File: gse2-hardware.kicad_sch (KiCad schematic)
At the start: 77 parts, among them J1 PJ-002A, J16 ARM, J17 ALARM, J2 PJ-002A, J3 ARM Cortex Debug, J31 Conn_02x09_Top_Bottom, J4 USB-C, Q15 DMG3402L, U27 USBLC6-2SC6, U36 MP2338GTL-Z, Y1 16MHz

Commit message: GSE v2.1: Updates for DSUB connectors for schematic only done. Layout needs a ton of work
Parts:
- removed D1: SDT8A100P5-7, Diode_SMD:D_PowerDI-5, symbol Device:D_Schottky_Small
- removed J17: ALARM, 0UCIRP-KiCAD-Lib:GX-16 2 pin, symbol Connector:Conn_01x02_Pin
- added C27: 0.1uF, Capacitor_SMD:C_0603_1608Metric, symbol Device:C_Small
- added C28: 100nF, Capacitor_SMD:C_0603_1608Metric, symbol Device:C_Small
- added D3: FSV8100V, Diode_SMD:D_PowerDI-5, symbol Device:D_Schottky_Small
- added J47: DSUB_15pin/VGA Veritical Female, 0UCIRP-KiCAD-Lib:Connector_VGA_Vertical, symbol 0UCIRP-KiCAD-Lib:Connector_VGA_vertical
- added R23, R24: 0R, Resistor_SMD:R_1210_3225Metric_Pad1.30x2.65mm_HandSolder, symbol Device:R_Small_US
- added R26: 2k, Resistor_SMD:R_0603_1608Metric, symbol Device:R_Small_US
- added U8: MAX11614, Package_SO:QSOP-16_3.9x4.9mm_P0.635mm, symbol Analog_ADC:MAX11614
- D4: value SDT8A100P5-7 -> FSV8100V
- F1: value ~ -> 3568
- J7: renamed from J31; value Conn_02x09_Top_Bottom -> 0430451812
- U1: renamed from U2; value ~ -> STM32F105RCT6
- U2: renamed from U33; value ~ -> AS78L05RTR-E1
- U6: renamed from U26; value ~ -> UA78M10CKVURG3
- U7: renamed from U30; value ~ -> BA78M20FP-E2
- renumbered C9 to C10, C44 to C11, C69 to C12, C98 to C13, C99 to C14, C70 to C15, C100 to C16, C15 to C17, C101 to C18, C45 to C19, C46 to C20, C102 to C21, C47 to C22, C103 to C23, C48 to C24, C104 to C25, C28 to C26, C10 to C3, C3 to C4, C4 to C5, C5 to C6, C6 to C7, C7 to C8, C8 to C9, D5 to D1, D6 to D2, D26 to D5, D42 to D6, J16 to J6, L2 to L1, Q15 to Q1, R9 to R1, R66 to R10, R67 to R11, R73 to R12, R64 to R13, R65 to R14, R69 to R17, R70 to R18, R71 to R19, R82 to R2, R62 to R20, R63 to R21, R68 to R22, R72 to R25, R83 to R3, R2 to R4, R3 to R5, R7 to R6, R104 to R7, R10 to R8, R8 to R9, U27 to U3, U36 to U5
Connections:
- net +24V: now also J47.1, J47.2, J47.3, J47.4, J47.5
- net +5V: now also C28.1, U8.16 (Vdd)
- net ETH_RX: now also U1.30 (PB11), U4.4 (TX); no longer U1.29 (PB10), U4.5 (RX)
- net ETH_TX: now also U1.29 (PB10), U4.5 (RX); no longer U1.30 (PB11), U4.4 (TX)
- net GND: now also C27.1, C28.2, U8.15 (GND)
- net SOLENOID0_EN: now also U1.4 (PC15); no longer U1.56 (PB4)
- net SOLENOID1_EN: now also U1.3 (PC14); no longer U1.57 (PB5)
- net SOLENOID2_EN: now also U1.2 (PC13); no longer U1.58 (PB6)
- net SOLENOID3_EN: now also U1.62 (PB9); no longer U1.59 (PB7)
- net SOLENOID5_EN: now also U1.57 (PB5); no longer U1.62 (PB9)
- net SOLENOID6_EN: now also U1.56 (PB4); no longer U1.2 (PC13)
- net SOLENOID7_EN: now also U1.55 (PB3); no longer U1.3 (PC14)
- net SOLENOID7_FB: now also U1.17 (PA3); no longer U1.20 (PA4)
- net SOLENOID8_EN: now also U1.54 (PD2); no longer U1.4 (PC15)
- net SOLENOID8_FB: now also U1.20 (PA4); no longer U1.17 (PA3)
- net at J1.1, R4.2, R8.2: now also D3.2 (A)
- net SOLENOID9_EN: now reaches U1.53 (PC12)
- net at D4.1 (K), F1.1: now also D3.1 (K)
- net at Q1.3 (D): now also J47.10, J47.6, J47.7, J47.8, J47.9
- net LC0_AI+ renamed NI_PT1_read
- net LC0_AI- renamed NI_PT9_read
- net LC1_AI+ renamed NI_PT0_read
- net LC1_AI- renamed NI_PT8_read
- net PT0_read renamed NI_PT10_read
- net PT10_read renamed NI_PT6_read
- net PT11_read renamed NI_PT7_read
- net PT1_read renamed NI_PT11_read
- net PT2_read renamed NI_PT12_read
- net PT3_read renamed NI_PT13_read
- net PT4_read: no longer names the net of J7.16 (Pin_16)
- net PT4_read: now also R23.2, R24.2
- net PT5_read renamed LoadCell0_read
- net PT6_read renamed NI_PT2_read
- net PT7_read renamed NI_PT3_read
- net PT8_read renamed NI_PT4_read
- net PT9_read renamed NI_PT5_read
- net TC_POCI renamed TC_MISO
- net V_SENSE0 renamed SOLENOID9_FB
- net V_SENSE1 renamed SOLENOID10_FB
- net V_SENSE2 renamed SOLENOID11_FB
- net V_SENSE3 renamed SOLENOID10_EN
- net V_SENSE4 renamed SOLENOID11_EN
- new net: C27.2, R26.1
- new net: R26.2, U8.1 (REF)
- new net EXT_ADC_SCL: U1.58 (PB6), U8.13 (SCL)
- new net EXT_ADC_SDA: U1.59 (PB7), U8.14 (SDA)
- new net LoadCell1_read: R24.1
- new net NI_PT14_read: R23.1
- new net STM_PT0_read: U8.5 (AIN0)
- new net STM_PT1_read: U8.6 (AIN1)
- new net STM_PT2_read: U8.7 (AIN2)
- new net STM_PT3_read: U8.8 (AIN3)
- new net STM_PT4_read: U8.9 (AIN4)
- new net STM_PT5_read: U8.10 (AIN5)
- new net STM_PT6_read: U8.11 (AIN6)
- new net STM_PT7_read: U8.12 (AIN7)
- no-connect marks 23 -> 26
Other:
- removed sheet LoadCell0
- removed sheet LoadCell1
- removed sheet Volt-Sense0
- removed sheet Volt-Sense1
- removed sheet Volt-Sense2
- removed sheet Volt-Sense3
- removed sheet Volt-Sense4
- added sheet Loadcell0 (loadcell.kicad_sch)
- added sheet Loadcell1 (loadcell.kicad_sch)
- added sheet PT12 (pt.kicad_sch)
- added sheet PT13 (pt.kicad_sch)
- added sheet PT14 (pt.kicad_sch)
- added sheet STM_PT0 (pt.kicad_sch)
- added sheet STM_PT1 (pt.kicad_sch)
- added sheet STM_PT2 (pt.kicad_sch)
- added sheet STM_PT3 (pt.kicad_sch)
- added sheet STM_PT4 (pt.kicad_sch)
- added sheet STM_PT5 (pt.kicad_sch)
- added sheet STM_PT6 (pt.kicad_sch)
- added sheet STM_PT7 (pt.kicad_sch)
- added sheet Solenoid10 (solenoid.kicad_sch)
- added sheet Solenoid11 (solenoid.kicad_sch)
- added sheet Solenoid9 (solenoid.kicad_sch)
- sheet TC0 ports: added MISO; removed POCI
- sheet TC1 ports: added MISO; removed POCI
- sheet TC2 ports: added MISO; removed POCI
- note added: "For PTs, based on https://www.ni.com/en/shop/data-acquisition/measurement -fundamentals/field-wiring-and-noise-considerations-for -analog-signals.html"
- note added: "SPI3"
- note added: "USART3"
- note removed: "For PTs, based on https://www.ni.com/en/shop/data-acquisition/measurement -fundamentals/field-wiring-and-noise-considerations-for-analog-signals.html"
- moved on the sheet: C11, C17, J3, J6, Q1, R13, R14, R20, R21, U4, Y1

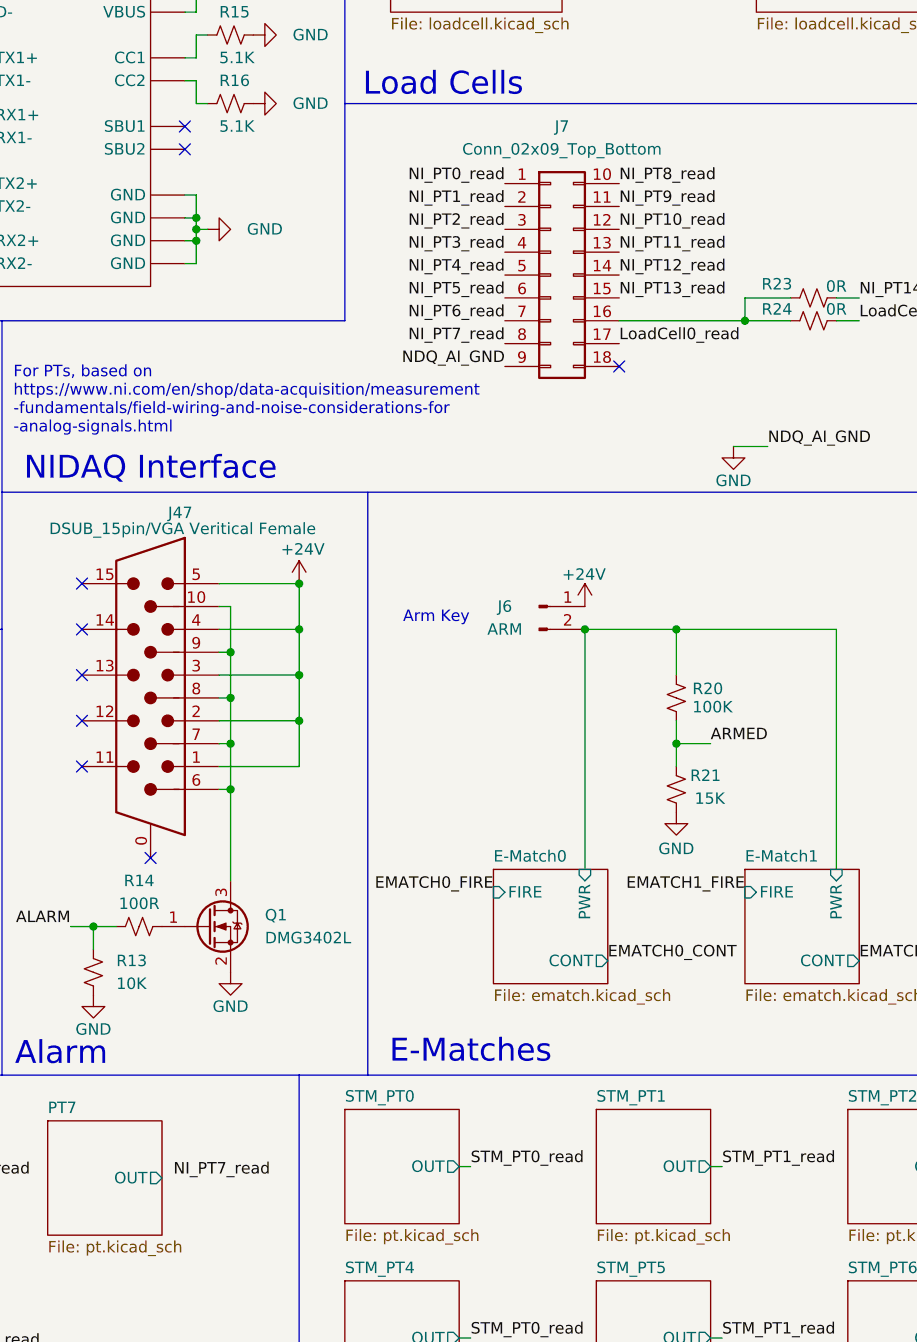
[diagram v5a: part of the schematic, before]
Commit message: GSE v2.1: routing for NI stuff done, need to do a lot of stm32 and power routing now
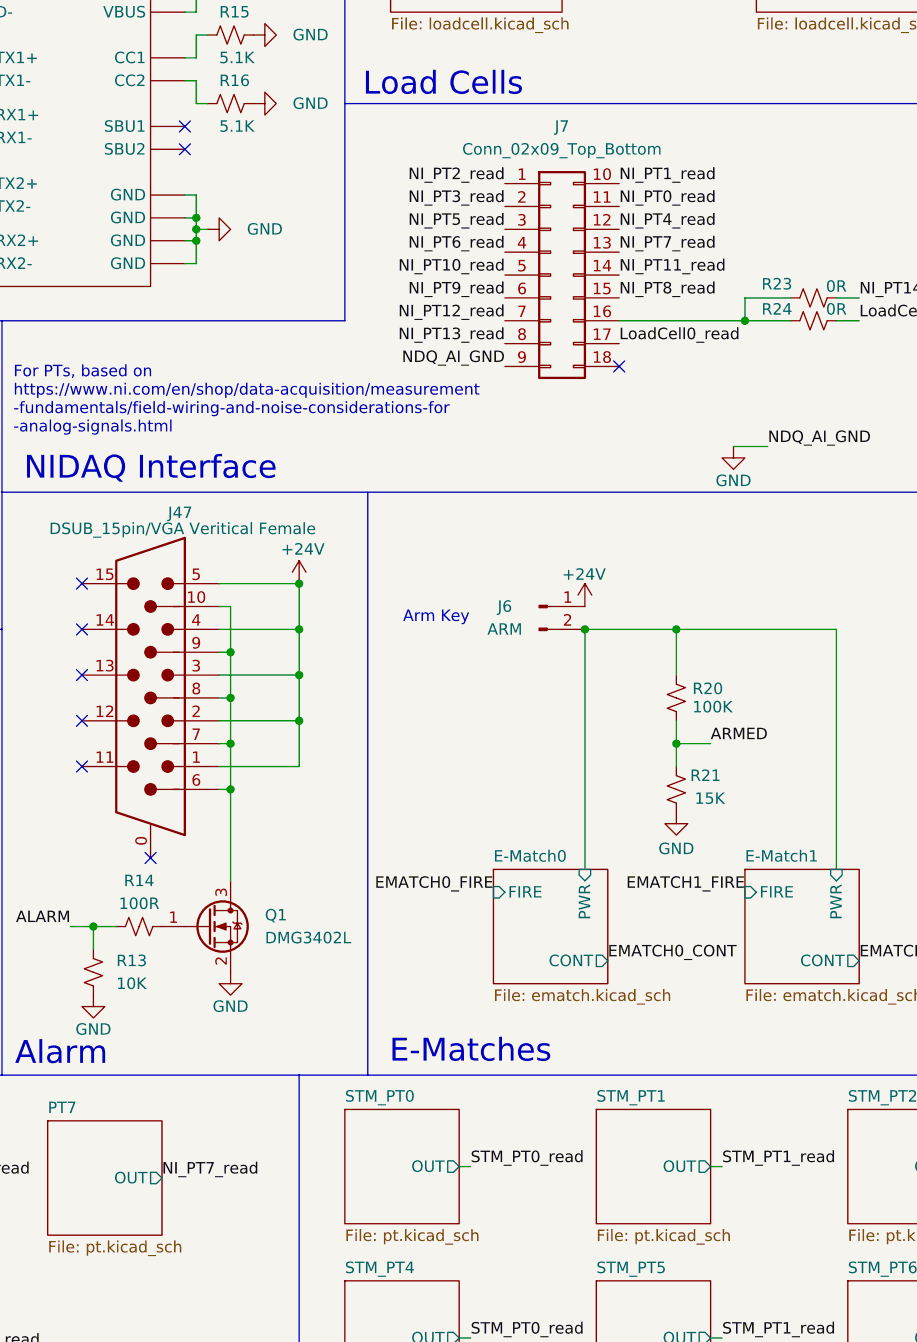
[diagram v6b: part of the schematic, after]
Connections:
- net NI_PT0_read: now also J7.11 (Pin_11); no longer J7.1 (Pin_1)
- net NI_PT10_read: now also J7.5 (Pin_5); no longer J7.12 (Pin_12)
- net NI_PT11_read: now also J7.14 (Pin_14); no longer J7.13 (Pin_13)
- net NI_PT12_read: now also J7.7 (Pin_7); no longer J7.14 (Pin_14)
- net NI_PT13_read: now also J7.8 (Pin_8); no longer J7.15 (Pin_15)
- net NI_PT1_read: now also J7.10 (Pin_10); no longer J7.2 (Pin_2)
- net NI_PT2_read: now also J7.1 (Pin_1); no longer J7.3 (Pin_3)
- net NI_PT3_read: now also J7.2 (Pin_2); no longer J7.4 (Pin_4)
- net NI_PT4_read: now also J7.12 (Pin_12); no longer J7.5 (Pin_5)
- net NI_PT5_read: now also J7.3 (Pin_3); no longer J7.6 (Pin_6)
- net NI_PT6_read: now also J7.4 (Pin_4); no longer J7.7 (Pin_7)
- net NI_PT7_read: now also J7.13 (Pin_13); no longer J7.8 (Pin_8)
- net NI_PT8_read: now also J7.15 (Pin_15); no longer J7.10 (Pin_10)
- net NI_PT9_read: now also J7.6 (Pin_6); no longer J7.11 (Pin_11)
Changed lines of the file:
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@@
+		)
+	)
+	(label "NI_PT12_read"
+		(at 250.19 66.04 180)
+		(effects
+			(font
+				(size 1.27 1.27)
+			)
+			(justify right bottom)
 		)
 	)
@@
 		)
 	)
+	(label "NI_PT8_read"
+		(at 262.89 63.5 0)
+		(effects
+			(font
+				(size 1.27 1.27)
+			)
+			(justify left bottom)
+		)
+	)
 	(label "SOLENOID8_EN"
 		(at 101.6 101.6 0)
@@
 		)
 	)
+	(label "NI_PT10_read"
+		(at 250.19 60.96 180)
+		(effects
+			(font
+				(size 1.27 1.27)
+			)
+			(justify right bottom)
+		)
+	)
 	(label "SOLENOID11_EN"
 		(at 382.27 129.54 180)
@@
 		)
 	)
-	(label "NI_PT12_read"
-		(at 262.89 60.96 0)
-		(effects
-			(font
-				(size 1.27 1.27)
-			)
-			(justify left bottom)
-		)
-	)
 	(label "NI_PT9_read"
 		(at 52.07 180.34 0)
@@
 		)
 	)
+	(label "NI_PT4_read"
+		(at 262.89 55.88 0)
+		(effects
+			(font
+				(size 1.27 1.27)
+			)
+			(justify left bottom)
+		)
+	)
 	(label "PWR0"
 		(at 38.1 223.52 180)
@@
 		)
 	)
-	(label "NI_PT5_read"
-		(at 250.19 63.5 180)
-		(effects
-			(font
-				(size 1.27 1.27)
-			)
-			(justify right bottom)
-		)
-	)
 	(label "USB_D-"
 		(at 55.88 82.55 180)
@@
 		)
 	)
+	(label "NI_PT5_read"
+		(at 250.19 55.88 180)
+		(effects
+			(font
+				(size 1.27 1.27)
+			)
+			(justify right bottom)
+		)
+	)
 	(label "STM_PT1_read"
 		(at 274.32 179.07 0)
@@
 		)
 	)
-	(label "NI_PT13_read"
-		(at 262.89 63.5 0)
-		(effects
-			(font
-				(size 1.27 1.27)
-			)
-			(justify left bottom)
+	(label "NI_PT3_read"
+		(at 250.19 53.34 180)
+		(effects
+			(font
+				(size 1.27 1.27)
+			)
+			(justify right bottom)
 		)
 	)
@@
 		)
 	)
-	(label "NI_PT9_read"
-		(at 262.89 53.34 0)
-		(effects
-			(font
-				(size 1.27 1.27)
-			)
-			(justify left bottom)
-		)
-	)
 	(label "NI_PT13_read"
 		(at 158.75 180.34 0)
@@
 		)
 	)
-	(label "NI_PT3_read"
-		(at 250.19 58.42 180)
+	(label "NI_PT1_read"
+		(at 262.89 50.8 0)
+		(effects
+			(font
+				(size 1.27 1.27)
+			)
+			(justify left bottom)
+		)
+	)
+	(label "NI_PT9_read"
+		(at 250.19 63.5 180)
 		(effects
 			(font
@@
 		)
 	)
-	(label "NI_PT0_read"
-		(at 250.19 50.8 180)
-		(effects
-			(font
-				(size 1.27 1.27)
-			)
-			(justify right bottom)
-		)
-	)
 	(label "STM_PT0_read"
 		(at 246.38 160.02 0)
@@
 		)
 	)
+	(label "NI_PT2_read"
+		(at 250.19 50.8 180)
+		(effects
+			(font
+				(size 1.27 1.27)
+			)
+			(justify right bottom)
+		)
+	)
 	(label "SOLENOID2_FB"
 		(at 55.88 101.6 180)
@@
 		)
 	)
+	(label "NI_PT13_read"
+		(at 250.19 68.58 180)
+		(effects
+			(font
+				(size 1.27 1.27)
+			)
+			(justify right bottom)
+		)
+	)
 	(label "ETH_RX"
 		(at 101.6 82.55 0)
@@
 		)
 	)
-	(label "NI_PT11_read"
-		(at 262.89 58.42 0)
+	(label "NI_PT0_read"
+		(at 262.89 53.34 0)
 		(effects
 			(font
@@
 		)
 	)
-	(label "NI_PT6_read"
-		(at 250.19 66.04 180)
-		(effects
-			(font
-				(size 1.27 1.27)
-			)
-			(justify right bottom)
-		)
-	)
 	(label "TC1_~{CS}"
 		(at 358.14 20.32 180)
@@
 		)
 	)
+	(label "NI_PT6_read"
+		(at 250.19 58.42 180)
+		(effects
+			(font
+				(size 1.27 1.27)
+			)
+			(justify right bottom)
+		)
+	)
 	(label "SOLENOID9_EN"
 		(at 321.31 129.54 180)
@@
 		)
 	)
-	(label "NI_PT8_read"
-		(at 262.89 50.8 0)
-		(effects
-			(font
-				(size 1.27 1.27)
-			)
-			(justify left bottom)
-		)
-	)
 	(label "NI_PT4_read"
 		(at 130.81 161.29 0)
@@
 		)
 	)
+	(label "NI_PT7_read"
+		(at 262.89 58.42 0)
+		(effects
+			(font
+				(size 1.27 1.27)
+			)
+			(justify left bottom)
+		)
+	)
 	(label "SOLENOID2_EN"
 		(at 379.73 53.34 180)
@@
 	)
 	(label "NI_PT7_read"
-		(at 213.36 161.29 0)
+		(at 212.09 161.29 0)
 		(effects
 			(font
@@
 		)
 	)
-	(label "NI_PT1_read"
-		(at 250.19 53.34 180)
-		(effects
-			(font
-				(size 1.27 1.27)
-			)
-			(justify right bottom)
-		)
-	)
-	(label "NI_PT4_read"
-		(at 250.19 60.96 180)
-		(effects
-			(font
-				(size 1.27 1.27)
-			)
-			(justify right bottom)
-		)
-	)
 	(label "SOLENOID6_EN"
 		(at 321.31 104.14 180)
@@
 		)
 	)
-	(label "NI_PT10_read"
-		(at 262.89 55.88 0)
-		(effects
-			(font
-				(size 1.27 1.27)
-			)
-			(justify left bottom)
-		)
-	)
 	(label "NI_PT6_read"
 		(at 186.69 161.29 0)
@@
 		)
 	)
-	(label "NI_PT2_read"
-		(at 250.19 55.88 180)
-		(effects
-			(font
-				(size 1.27 1.27)
-			)
-			(justify right bottom)
-		)
-	)
 	(label "SOLENOID4_FB"
 		(at 55.88 54.61 180)
@@
 		)
 	)
-	(label "NI_PT7_read"
-		(at 250.19 68.58 180)
-		(effects
-			(font
-				(size 1.27 1.27)
-			)
-			(justify right bottom)
-		)
-	)
 	(label "TC_MISO"
 		(at 344.17 27.94 0)
@@
 		(effects
 			(font
+				(size 1.27 1.27)
+			)
+			(justify left bottom)
+		)
+	)
+	(label "NI_PT11_read"
+		(at 262.89 60.96 0)
+		(effects
+			(font
